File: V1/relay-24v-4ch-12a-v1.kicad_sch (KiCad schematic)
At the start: 22 parts, among them J1 DG141V-2.54-6P, J2 DB142V-5.08-8P, K1 G5PZ-1A, K2 G5PZ-1A, K3 G5PZ-1A, K4 G5PZ-1A

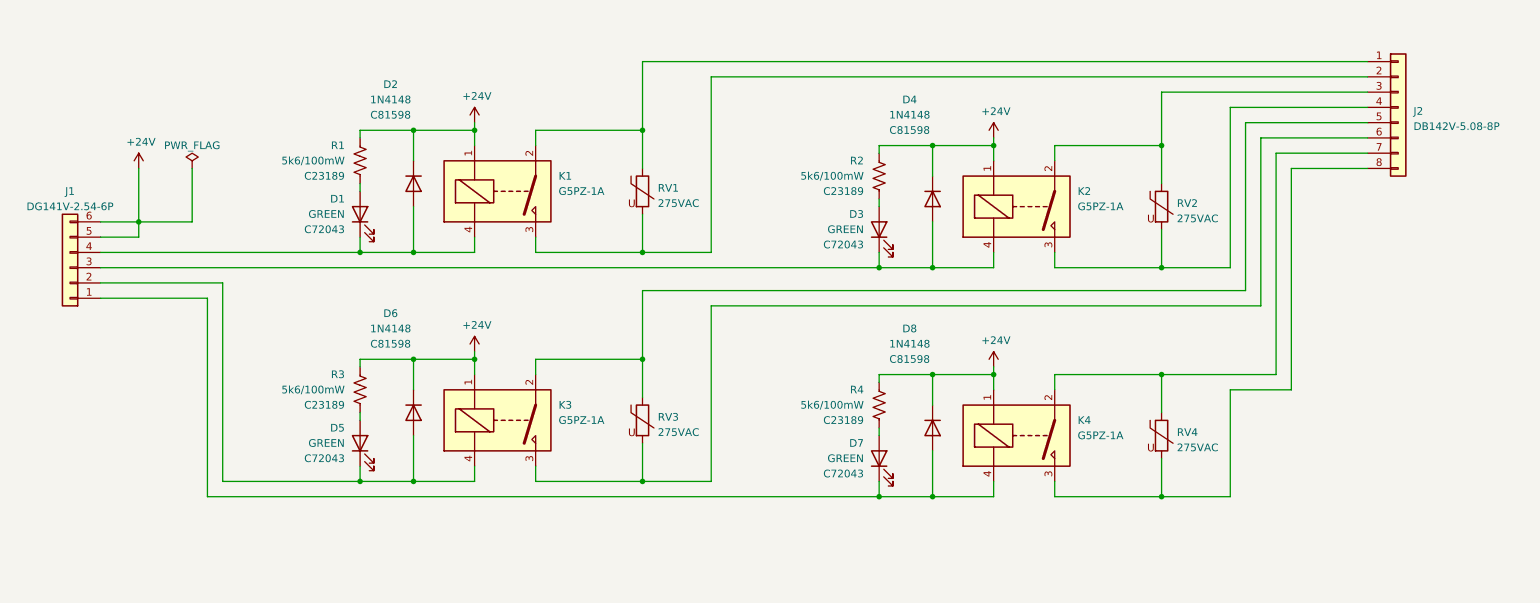
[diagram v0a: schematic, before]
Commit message: Updated connectors
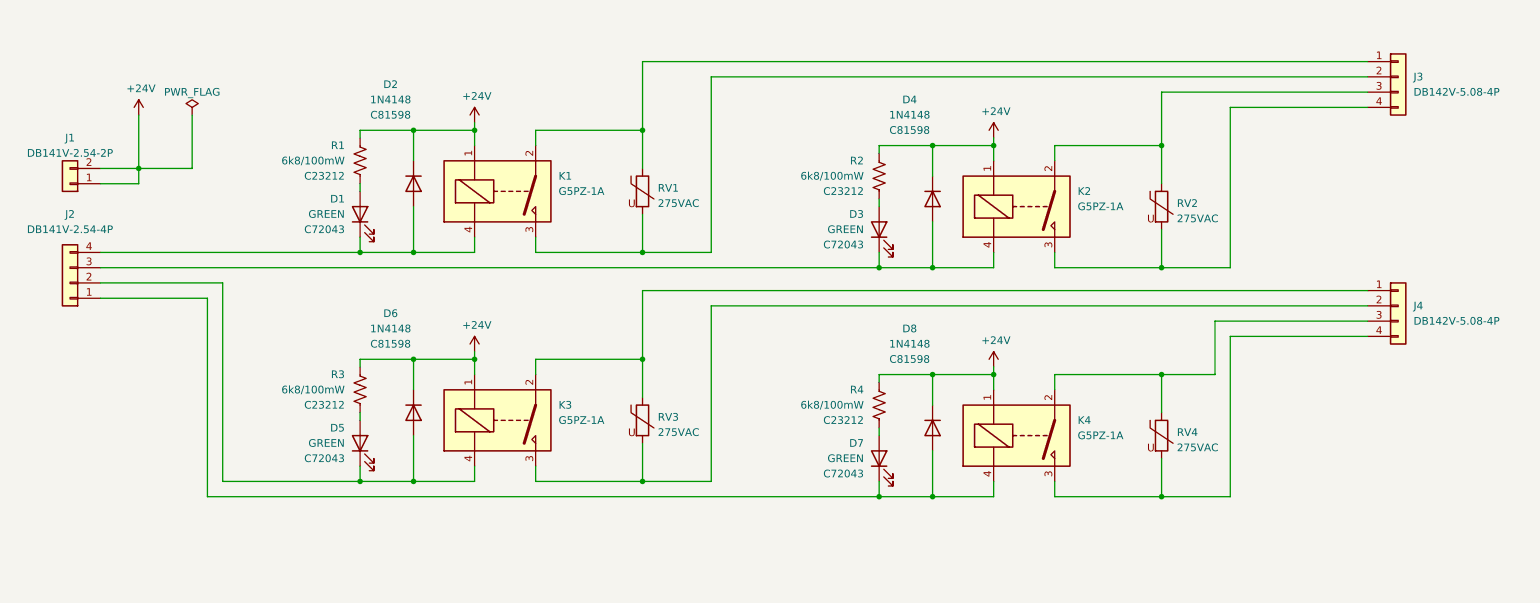
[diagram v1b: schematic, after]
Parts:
- removed J1: DG141V-2.54-6P, Tales:TerminalBlock_Dibo_DB141V-2.54-6P_1x06_P2.54mm_Vertical, symbol Connector_Generic:Conn_01x06
- removed J2: DB142V-5.08-8P, Tales:TerminalBlock_Dibo_DB142V-5.08-8P_1x08_P5.08mm_Vertical, symbol Connector_Generic:Conn_01x08
- added J1: DB141V-2.54-2P, Tales:TerminalBlock_Dibo_DB141V-2.54-2P_1x02_P2.54mm_Vertical, symbol Connector_Generic:Conn_01x02
- added J2: DB141V-2.54-4P, Tales:TerminalBlock_Dibo_DB141V-2.54-4P_1x04_P2.54mm_Vertical, symbol Connector_Generic:Conn_01x04
- added J3, J4: DB142V-5.08-4P, Tales:TerminalBlock_Dibo_DB142V-5.08-4P_1x04_P5.08mm_Vertical, symbol Connector_Generic:Conn_01x04
- R1, R2, R3, R4: value 5k6/100mW -> 6k8/100mW; LCSC Part # C23189 -> C23212; Mfr PN 0805W8F4701T5E -> 0603WAF6801T5E; Vendor PN C23189 -> C23212
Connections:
- net +24V: now also J1.1 (Pin_1), J1.2 (Pin_2)
- net at D7.1 (K), D8.2 (A), K4.4: now also J2.1 (Pin_1)
- net at K3.2, RV3.1: now also J4.1 (Pin_1)
- net at K3.3, RV3.2: now also J4.2 (Pin_2)
- net at D5.1 (K), D6.2 (A), K3.4: now also J2.2 (Pin_2)
- net at D1.1 (K), D2.2 (A), K1.4: now also J2.4 (Pin_4)
- net at D3.1 (K), D4.2 (A), K2.4: now also J2.3 (Pin_3)
- net at K4.2, RV4.1: now also J4.3 (Pin_3)
- net at K4.3, RV4.2: now also J4.4 (Pin_4)
- net at K1.2, RV1.1: now also J3.1 (Pin_1)
- net at K1.3, RV1.2: now also J3.2 (Pin_2)
- net at K2.2, RV2.1: now also J3.3 (Pin_3)
- net at K2.3, RV2.2: now also J3.4 (Pin_4)

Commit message: Revision before manufacturing
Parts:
- D1, D3, D5, D7: value GREEN -> WHITE; LCSC Part # C72043 -> C2290; Mfr Everlight -> Hubei KENTO Elec; Mfr PN 19-217/GHC-YR1S2/3T -> KT-0603W; Vendor PN C72043 -> C2290
- R1, R2, R3, R4: value 6k8/100mW -> 10k/100mW; LCSC Part # C23212 -> C25804; Mfr Uniroyal -> UNI-ROYAL(Uniroyal Elec); Mfr PN 0603WAF6801T5E -> 0603WAF1002T5E; Vendor PN C23212 -> C25804
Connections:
- net IN4: now reaches D7.1 (K), D8.2 (A), J2.1 (Pin_1), K4.4
- net LED4: now reaches D7.2 (A), R4.2
- net OUT3PW: now reaches J4.1 (Pin_1), K3.2, RV3.1
- net OUT3LD: now reaches J4.2 (Pin_2), K3.3, RV3.2
- net IN3: now reaches D5.1 (K), D6.2 (A), J2.2 (Pin_2), K3.4
- net IN1: now reaches D1.1 (K), D2.2 (A), J2.4 (Pin_4), K1.4
- net OUT1PW: now reaches J3.1 (Pin_1), K1.2, RV1.1
- net OUT1LD: now reaches J3.2 (Pin_2), K1.3, RV1.2
- net OUT2PW: now reaches J3.3 (Pin_3), K2.2, RV2.1
- net OUT2LD: now reaches J3.4 (Pin_4), K2.3, RV2.2
- net LED1: now reaches D1.2 (A), R1.2
- net LED3: now reaches D5.2 (A), R3.2
- net OUT4PW: now reaches J4.3 (Pin_3), K4.2, RV4.1
- net OUT4LD: now reaches J4.4 (Pin_4), K4.3, RV4.2
- net IN2: now reaches D3.1 (K), D4.2 (A), J2.3 (Pin_3), K2.4
- net LED2: now reaches D3.2 (A), R2.2
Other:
- moved on the sheet: D1, D2, D3, D4, D5, D6, D7, D8, J4, K1, K2, K3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

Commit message: Review before fabrication
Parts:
- J1: LCSC Part # (none) -> C2898744; Mfr (none) -> DORABO; Mfr PN (none) -> DB141V-2.54-2P-GN; Vendor PN (none) -> C2898744
- J2: LCSC Part # (none) -> C2898746; Mfr (none) -> DORABO; Mfr PN (none) -> DB141V-2.54-4P-GN; Vendor PN (none) -> C2898746
- K1, K2, K3, K4: JLCPCB BOM 0 -> 1; LCSC Part # (none) -> C6719448; Mfr PN G5PZ-1A -> G5PZ-1A-E DC24V; Vendor Mouser -> JLCPCB; Vendor PN 653-G5PZ-1ADC24 -> C6719448
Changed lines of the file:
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@@
 			)
 		)
-		(property "Mfr PN" "G5PZ-1A"
+		(property "Mfr PN" "G5PZ-1A-E DC24V"
 			(at 107.95 127 0)
 			(effects
@@
 			)
 		)
-		(property "Vendor" "Mouser"
+		(property "Vendor" "JLCPCB"
 			(at 107.95 127 0)
 			(effects
@@
 			)
 		)
-		(property "Vendor PN" "653-G5PZ-1ADC24"
+		(property "Vendor PN" "C6719448"
 			(at 107.95 127 0)
 			(effects
@@
 			)
 		)
-		(property "JLCPCB BOM" "0"
+		(property "JLCPCB BOM" "1"
 			(at 107.95 127 0)
 			(effects
@@
 			)
 		)
+		(property "LCSC Part #" "C6719448"
+			(at 121.92 129.54 0)
+			(effects
+				(font
+					(size 1.27 1.27)
+				)
+			)
+		)
 		(pin "1"
 		)
@@
 			)
 		)
-		(property "Mfr PN" "G5PZ-1A"
+		(property "Mfr PN" "G5PZ-1A-E DC24V"
 			(at 194.31 128.27 0)
 			(effects
@@
 			)
 		)
-		(property "Vendor" "Mouser"
+		(property "Vendor" "JLCPCB"
 			(at 194.31 128.27 0)
 			(effects
@@
 			)
 		)
-		(property "Vendor PN" "653-G5PZ-1ADC24"
+		(property "Vendor PN" "C6719448"
 			(at 194.31 128.27 0)
 			(effects
@@
 			)
 		)
-		(property "JLCPCB BOM" "0"
+		(property "JLCPCB BOM" "1"
 			(at 194.31 128.27 0)
 			(effects
@@
 			)
 		)
+		(property "LCSC Part #" "C6719448"
+			(at 208.28 130.81 0)
+			(effects
+				(font
+					(size 1.27 1.27)
+				)
+			)
+		)
 		(pin "1"
 		)
@@
 			)
 		)
-		(property "Mfr PN" "G5PZ-1A"
+		(property "Mfr PN" "G5PZ-1A-E DC24V"
 			(at 107.95 73.66 0)
 			(effects
@@
 			)
 		)
-		(property "Vendor" "Mouser"
+		(property "Vendor" "JLCPCB"
 			(at 107.95 73.66 0)
 			(effects
@@
 			)
 		)
-		(property "Vendor PN" "653-G5PZ-1ADC24"
+		(property "Vendor PN" "C6719448"
 			(at 107.95 73.66 0)
 			(effects
@@
 			)
 		)
-		(property "JLCPCB BOM" "0"
+		(property "JLCPCB BOM" "1"
 			(at 107.95 73.66 0)
 			(effects
@@
 			)
 		)
+		(property "LCSC Part #" "C6719448"
+			(at 121.92 76.2 0)
+			(effects
+				(font
+					(size 1.27 1.27)
+				)
+			)
+		)
 		(pin "1"
 		)
@@
 			)
 		)
+		(property "LCSC Part #" "C2898746"
+			(at 35.56 91.44 0)
+			(effects
+				(font
+					(size 1.27 1.27)
+				)
+				(hide yes)
+			)
+		)
+		(property "Mfr" "DORABO"
+			(at 35.56 91.44 0)
+			(effects
+				(font
+					(size 1.27 1.27)
+				)
+				(hide yes)
+			)
+		)
+		(property "Mfr PN" "DB141V-2.54-4P-GN"
+			(at 35.56 91.44 0)
+			(effects
+				(font
+					(size 1.27 1.27)
+				)
+				(hide yes)
+			)
+		)
+		(property "Vendor PN" "C2898746"
+			(at 35.56 91.44 0)
+			(effects
+				(font
+					(size 1.27 1.27)
+				)
+				(hide yes)
+			)
+		)
 		(pin "4"
 		)
@@
 			)
 		)
+		(property "LCSC Part #" "C2898744"
+			(at 35.56 74.93 0)
+			(effects
+				(font
+					(size 1.27 1.27)
+				)
+				(hide yes)
+			)
+		)
+		(property "Mfr" "DORABO"
+			(at 35.56 74.93 0)
+			(effects
+				(font
+					(size 1.27 1.27)
+				)
+				(hide yes)
+			)
+		)
+		(property "Mfr PN" "DB141V-2.54-2P-GN"
+			(at 35.56 74.93 0)
+			(effects
+				(font
+					(size 1.27 1.27)
+				)
+				(hide yes)
+			)
+		)
+		(property "Vendor PN" "C2898744"
+			(at 35.56 74.93 0)
+			(effects
+				(font
+					(size 1.27 1.27)
+				)
+				(hide yes)
+			)
+		)
 		(pin "2"
 		)
@@
 			)
 		)
-		(property "Mfr PN" "G5PZ-1A"
+		(property "Mfr PN" "G5PZ-1A-E DC24V"
 			(at 194.31 74.93 0)
 			(effects
@@
 			)
 		)
-		(property "Vendor" "Mouser"
+		(property "Vendor" "JLCPCB"
 			(at 194.31 74.93 0)
 			(effects
@@
 			)
 		)
-		(property "Vendor PN" "653-G5PZ-1ADC24"
+		(property "Vendor PN" "C6719448"
 			(at 194.31 74.93 0)
 			(effects
@@
 			)
 		)
-		(property "JLCPCB BOM" "0"
+		(property "JLCPCB BOM" "1"
 			(at 194.31 74.93 0)
 			(effects
@@
 			)
 		)
+		(property "LCSC Part #" "C6719448"
+			(at 208.28 77.47 0)
+			(effects
+				(font
+					(size 1.27 1.27)
+				)
+			)
+		)

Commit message: Revising before manufacturing.
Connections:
- net OUT1PW renamed OUT1LN
- net OUT2PW renamed OUT2LN
- net OUT3PW renamed OUT3LN
- net OUT4PW renamed OUT4LN
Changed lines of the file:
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@@
 		)
 	)
-	(label "OUT3PW"
+	(label "OUT3LN"
 		(at 241.3 107.95 0)
 		(effects
@@
 		)
 	)
-	(label "OUT4PW"
+	(label "OUT4LN"
 		(at 241.3 113.03 0)
 		(effects
@@
 		)
 	)
-	(label "OUT1PW"
+	(label "OUT1LN"
 		(at 241.3 54.61 0)
 		(effects
@@
 		)
 	)
-	(label "OUT2PW"
+	(label "OUT2LN"
 		(at 241.3 59.69 0)
 		(effects
